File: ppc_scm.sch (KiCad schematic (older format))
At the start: 0 parts

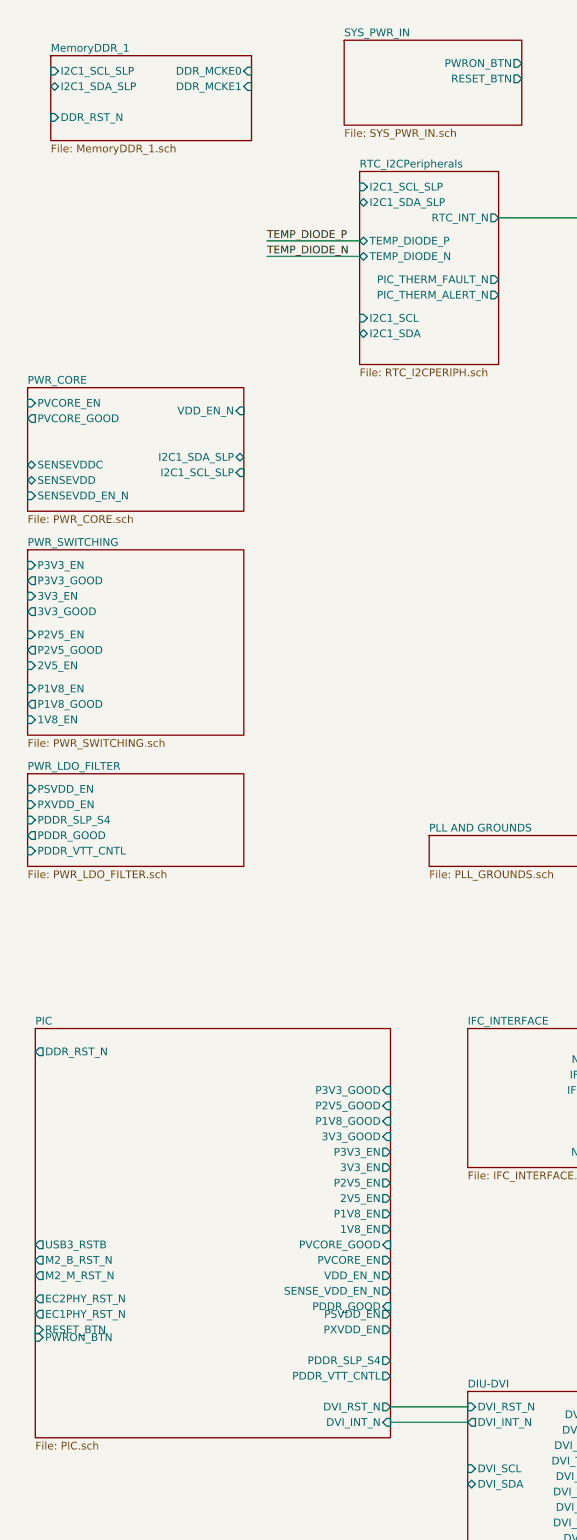
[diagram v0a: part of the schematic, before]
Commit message: work in progress on PIC and power enable net
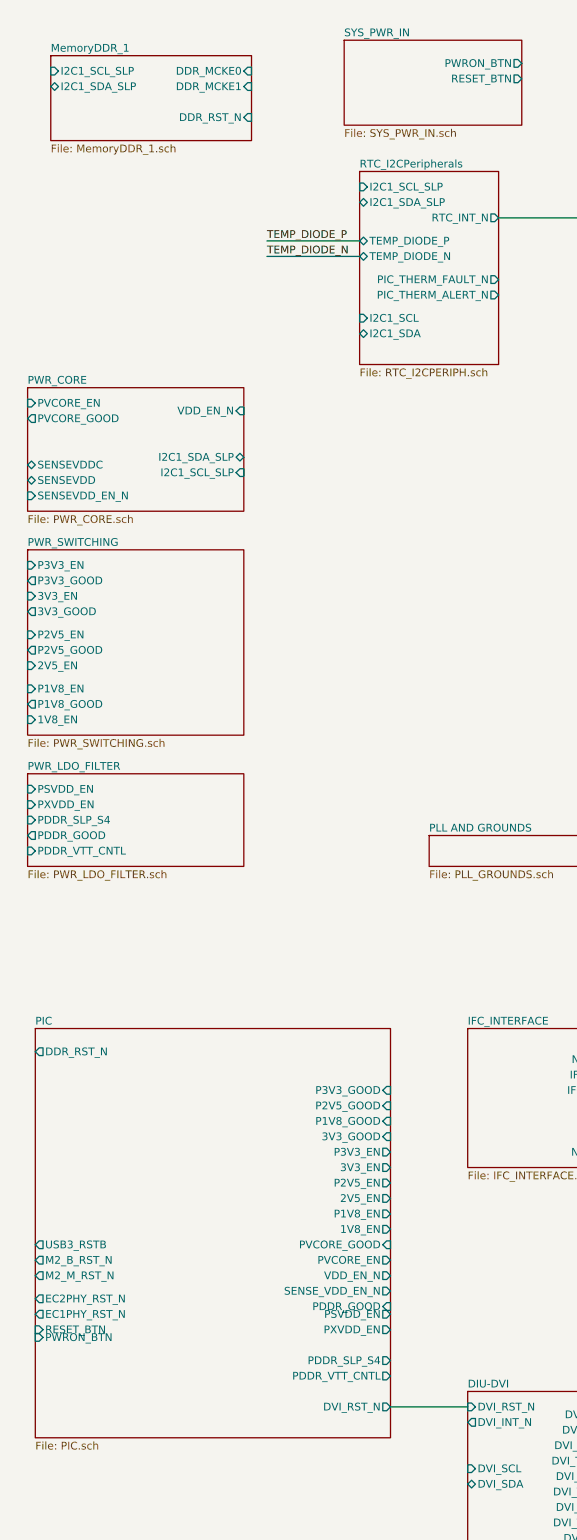
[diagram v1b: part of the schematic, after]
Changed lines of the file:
@@
 F4 "DDR_MCKE0" I R 2150 1300 50
 F5 "DDR_MCKE1" I R 2150 1400 50
-F6 "DDR_RST_N" I L 850 1600 50
+F6 "DDR_RST_N" I R 2150 1600 50
 $EndSheet
 $Sheet
@@
 Wire Wire Line
 	3550 9950 3050 9950
-Wire Wire Line
-	3050 10050 3550 10050
 $Sheet
 S 700  3350 1400 800
@@
 F2 "DDR_RST_N" O L 750 7650 50
 F3 "DVI_RST_N" O R 3050 9950 50
-F4 "DVI_INT_N" I R 3050 10050 50
-F5 "P3V3_GOOD" I R 3050 7900 50
-F6 "P2V5_GOOD" I R 3050 8000 50
-F7 "P1V8_GOOD" I R 3050 8100 50
-F8 "3V3_GOOD" I R 3050 8200 50
-F9 "P3V3_EN" O R 3050 8300 50
-F10 "3V3_EN" O R 3050 8400 50
-F11 "P2V5_EN" O R 3050 8500 50
-F12 "2V5_EN" O R 3050 8600 50
-F13 "P1V8_EN" O R 3050 8700 50
-F14 "1V8_EN" O R 3050 8800 50
-F15 "PVCORE_GOOD" I R 3050 8900 50
-F16 "PVCORE_EN" O R 3050 9000 50
-F17 "VDD_EN_N" O R 3050 9100 50
-F18 "SENSE_VDD_EN_N" O R 3050 9200 50
-F19 "PDDR_GOOD" I R 3050 9300 50
-F20 "PSVDD_EN" O R 3050 9350 50
-F21 "PXVDD_EN" O R 3050 9450 50
-F22 "PDDR_SLP_S4" O R 3050 9650 50
-F23 "PDDR_VTT_CNTL" O R 3050 9750 50
-F24 "PWRON_BTN" I L 750 9500 50
-F25 "RESET_BTN" I L 750 9450 50
-F26 "EC1PHY_RST_N" O L 750 9350 50
-F27 "EC2PHY_RST_N" O L 750 9250 50
-F28 "M2_M_RST_N" O L 750 9100 50
-F29 "M2_B_RST_N" O L 750 9000 50
-F30 "USB3_RSTB" O L 750 8900 50
+F4 "P3V3_GOOD" I R 3050 7900 50
+F5 "P2V5_GOOD" I R 3050 8000 50
+F6 "P1V8_GOOD" I R 3050 8100 50
+F7 "3V3_GOOD" I R 3050 8200 50
+F8 "P3V3_EN" O R 3050 8300 50
+F9 "3V3_EN" O R 3050 8400 50
+F10 "P2V5_EN" O R 3050 8500 50
+F11 "2V5_EN" O R 3050 8600 50
+F12 "P1V8_EN" O R 3050 8700 50
+F13 "1V8_EN" O R 3050 8800 50
+F14 "PVCORE_GOOD" I R 3050 8900 50
+F15 "PVCORE_EN" O R 3050 9000 50
+F16 "VDD_EN_N" O R 3050 9100 50
+F17 "SENSE_VDD_EN_N" O R 3050 9200 50
+F18 "PDDR_GOOD" I R 3050 9300 50
+F19 "PSVDD_EN" O R 3050 9350 50
+F20 "PXVDD_EN" O R 3050 9450 50
+F21 "PDDR_SLP_S4" O R 3050 9650 50
+F22 "PDDR_VTT_CNTL" O R 3050 9750 50
+F23 "PWRON_BTN" I L 750 9500 50
+F24 "RESET_BTN" I L 750 9450 50
+F25 "EC1PHY_RST_N" O L 750 9350 50
+F26 "EC2PHY_RST_N" O L 750 9250 50
+F27 "M2_M_RST_N" O L 750 9100 50
+F28 "M2_B_RST_N" O L 750 9000 50
+F29 "USB3_RSTB" O L 750 8900 50
 $EndSheet
 $EndSCHEMATC
